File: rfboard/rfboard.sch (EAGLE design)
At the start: 34 parts, among them Q1 IRLML5203, Q2 IRLML5203, Q3 IRLML5203, Q4 IRLML5203, Q5 IRLML5203

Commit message: Deleted voltage dividers, modified pinout
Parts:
- removed JP11, JP6, JP8: (no value), pinhead-2:PINHD-1X03_2.00
- removed JP4: (no value), SparkFun-Connectors:M06LOCK
- removed Q5: IRLML5203, ngohara_parts:IRLML5203
- removed R11, R12: (no value), resistor:R-US_R0805
- removed R1A, R1B, R2A, R2B, R3A, R3B: (no value), rcl:R-US_R1206
- added JP2: (no value), pinhead-2:PINHD-1X10_2.00
- added LSM_PWR, U$2: JST-PH2-SMD, jst-ph:JST-PH2-SMD
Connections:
- removed net DATA1: JP6.3, R1A.2
- removed net DATA2: JP8.3, R2A.2
- removed net DATA3: JP11.3, R3A.2
- removed net N$11: Q5.S, R12.2
- removed net N$12: Q5.D, R11.2
- removed net N$13: R11.1
- removed net N$14: Q5.G, R12.1
- removed net VD1: JP4.1, R1A.1, R1B.2
- removed net VD2: JP4.2, R2A.1, R2B.2
- removed net VD3: JP4.3, R3A.1, R3B.2
- net 3.3V: no longer JP11.2, JP6.2, JP8.2
- net GND: no longer JP11.1, JP6.1, JP8.1, R1B.1, R2B.1, R3B.1
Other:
- note removed: "Distance Sensors Voltage Division Circuit"
- moved on the sheet: 3.3V, 5V, C18, C19, JP1, JP5, X2

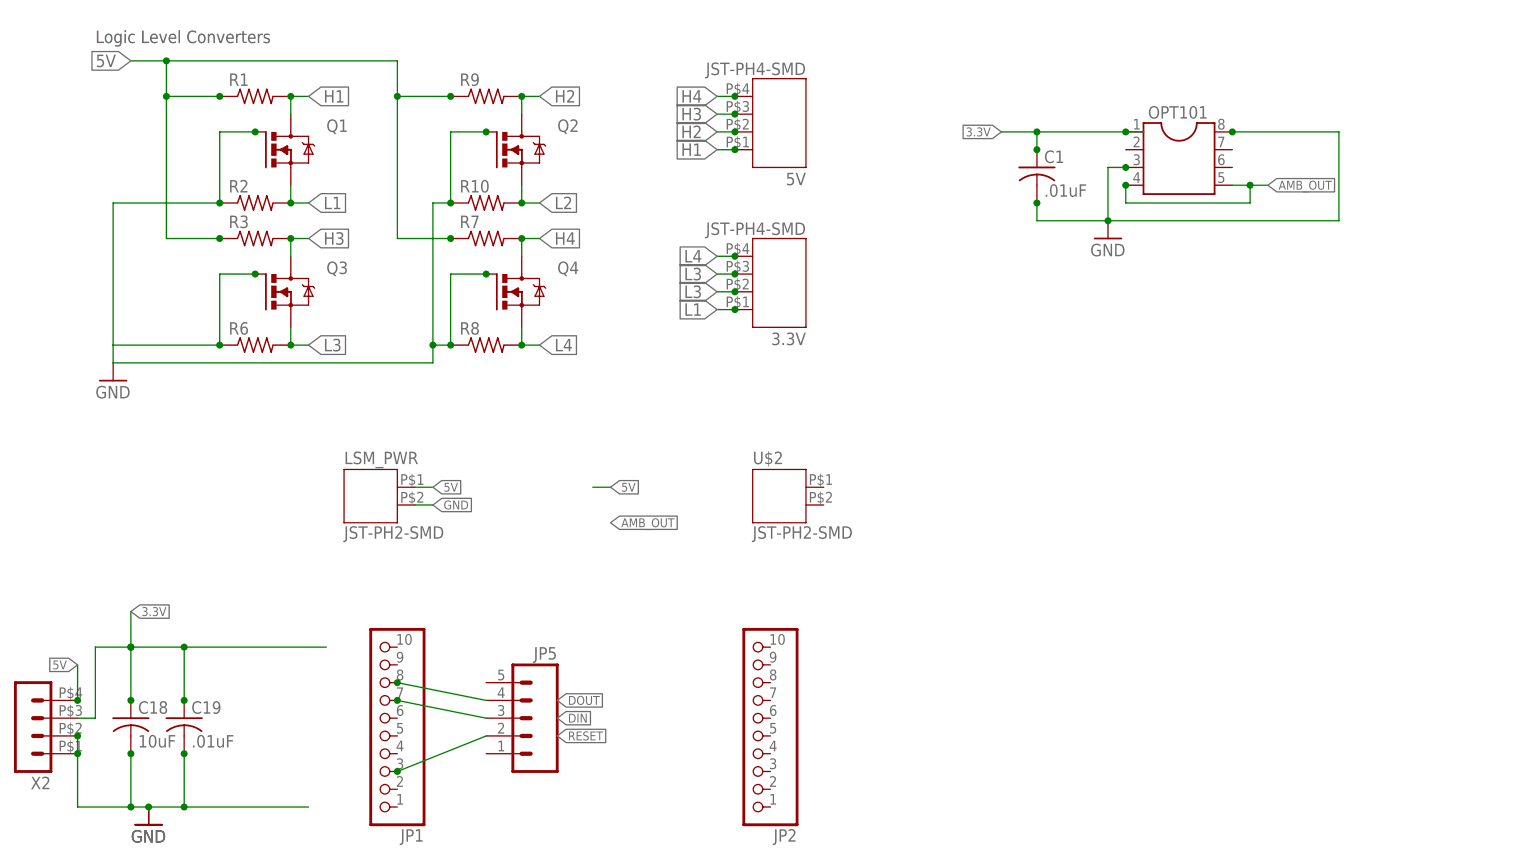
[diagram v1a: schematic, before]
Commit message: added voltage div to Amb_out, and amb_on fet
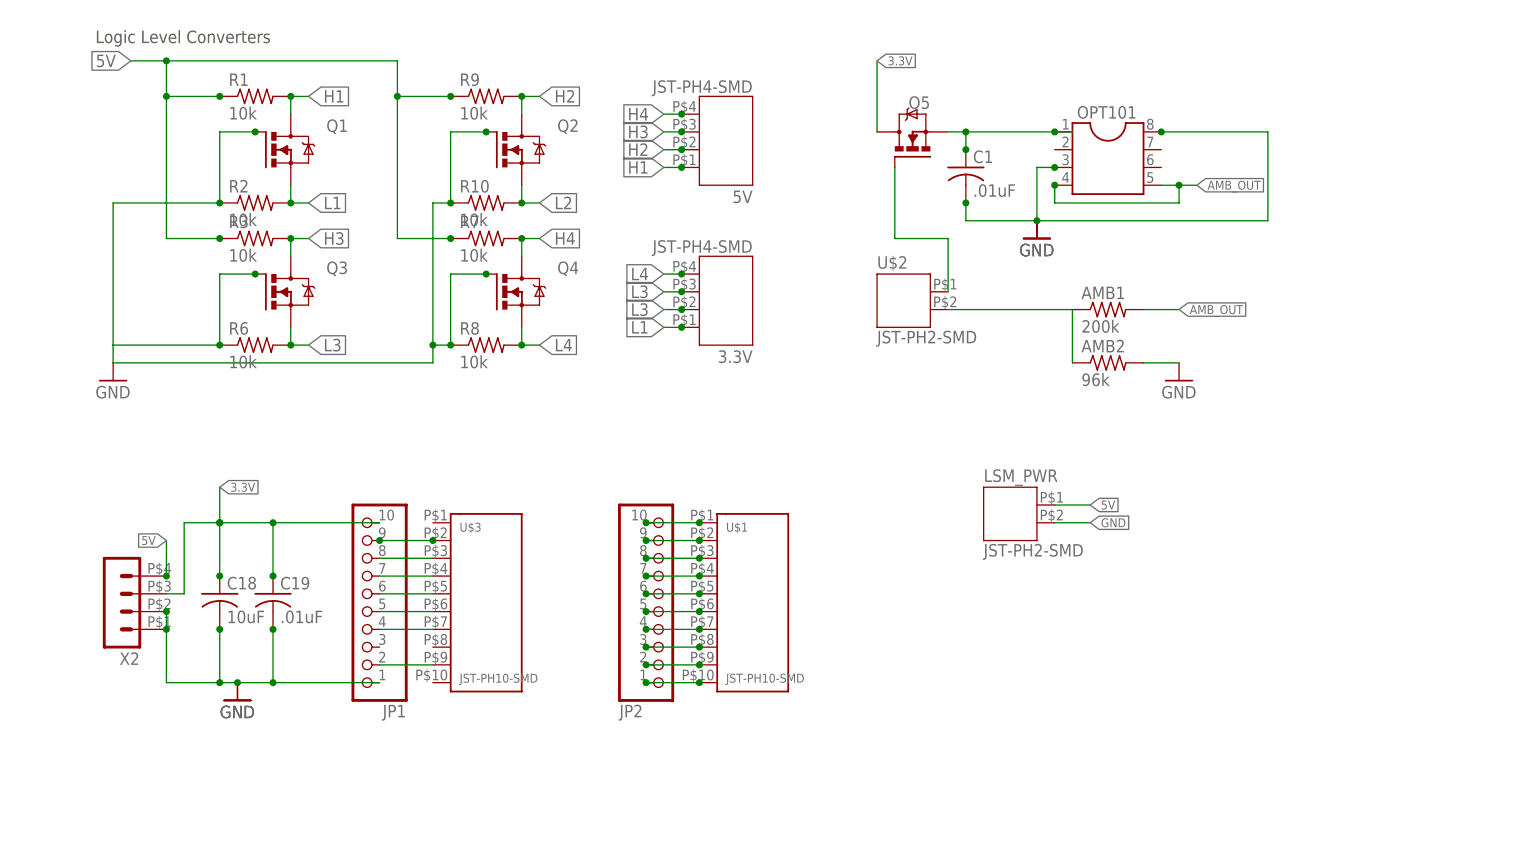
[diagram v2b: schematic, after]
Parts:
- removed JP5: (no value), SparkFun-Connectors:M05LOCK
- added AMB1: 200k, resistor:R-US_R0805
- added AMB2: 96k, resistor:R-US_R0805
- added Q5: IRLML5203, ngohara_parts:IRLML5203
- added U$1, U$3: JST-PH10-SMD, jst-ph:JST-PH10-SMD
- R1, R10, R2, R3, R6, R7, R8, R9: value (none) -> 10k
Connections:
- removed net DIN: JP1.7, JP5.3
- new net AD0/DI0: JP2.1, U$1.P$10
- new net AD1/DI1: JP2.2, U$1.P$9
- new net AD2/DI2: JP2.3, U$1.P$8
- new net AD3/D13: JP2.4, U$1.P$7
- new net AD4/DI4: JP2.10, U$1.P$1
- new net AMB_LOW: AMB1.1, AMB2.1
- new net AMB_ON: Q5.G, U$2.1
- new net ASS/AD5/DI5: JP2.6, U$1.P$5
- new net CTS/DI7: JP2.9, U$1.P$2
- new net DIN/CONFIG: JP1.8, U$3.P$3
- new net DO8: JP1.7, U$3.P$4
- new net DTR/SLEEP_RQ/D18: JP1.2, U$3.P$9
- new net ON/SLEEP: JP2.8, U$1.P$3
- new net PWM0/RSSI: JP1.5, U$3.P$6
- new net PWM1: JP1.4, U$3.P$7
- new net RST/AD6/DI6: JP2.5, U$1.P$6
- new net VREF: JP2.7, U$1.P$4
- net 3.3V: now also JP1.10, Q5.S
- net 5V: now also LSM_PWR.1
- net AMB_OUT: now also AMB1.2
- net DOUT: now also JP1.9, U$3.P$2; no longer JP1.8, JP5.4
- net GND: now also AMB2.2, JP1.1, LSM_PWR.2
- net RESET: now also JP1.6, U$3.P$5; no longer JP1.3, JP5.2
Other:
- moved on the sheet: 3.3V, 5V, C1, C18, C19, JP1, JP2, LSM_PWR, OPT101, U$2, X2

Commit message: finished laying board with components on bottom
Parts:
- renumbered X2 to X1
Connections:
- new net VIN: C1.1, OPT101.1, Q5.S
- net 3.3V: now also Q5.D, U$3.P$1; no longer C1.1, OPT101.1, Q5.S
- net AD0/DI0: now also U$1.P$1; no longer U$1.P$10
- net AD1/DI1: now also U$1.P$2; no longer U$1.P$9
- net AD2/DI2: now also U$1.P$3; no longer U$1.P$8
- net AD3/D13: now also U$1.P$4; no longer U$1.P$7
- net AD4/DI4: now also U$1.P$10; no longer U$1.P$1
- net AMB_LOW: now also U$2.2
- net ASS/AD5/DI5: now also U$1.P$6; no longer U$1.P$5
- net CTS/DI7: now also U$1.P$9; no longer U$1.P$2
- net GND: now also U$3.P$10
- net H1: now also 5V.4; no longer 5V.1
- net H2: now also 5V.3; no longer 5V.2
- net H3: now also 5V.2; no longer 5V.3
- net H4: now also 5V.1; no longer 5V.4
- net ON/SLEEP: now also U$1.P$8; no longer U$1.P$3
- net RST/AD6/DI6: now also U$1.P$5; no longer U$1.P$6
- net VREF: now also U$1.P$7; no longer U$1.P$4
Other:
- moved on the sheet: 5V, JP2, U$1, U$3

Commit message: Fixed fet Amb_On with resistors, fixed connector orientation, fixed text
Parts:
- added RGS: 2.2k, resistor:R-US_R0805
- added RIN: 10k, resistor:R-US_R0805
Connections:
- removed net VIN: C1.1, OPT101.1, Q5.S
- new net N$2: Q5.G, RGS.1, RIN.2
- new net N_GND: AMB2.2, C1.2, OPT101.3, OPT101.8, Q5.D
- net 3.3V: now also C1.1, OPT101.1, Q1.G, Q2.G, Q3.G, Q4.G, R10.1, R2.1, R6.1, R8.1; no longer Q5.D
- net AMB_ON: now also RIN.1; no longer Q5.G
- net GND: now also Q5.S, RGS.2; no longer AMB2.2, C1.2, OPT101.3, OPT101.8, Q1.G, Q2.G, Q3.G, Q4.G, R10.1, R2.1, R6.1, R8.1
- net L1: now also 3.3V.4; no longer 3.3V.1
- net L2: now also 3.3V.3; no longer 3.3V.2
- net L3: now also 3.3V.2; no longer 3.3V.3
- net L4: now also 3.3V.1; no longer 3.3V.4
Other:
- moved on the sheet: 3.3V, AMB1, AMB2, Q5, U$3
